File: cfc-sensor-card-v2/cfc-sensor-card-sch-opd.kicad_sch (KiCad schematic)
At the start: 69 parts, among them Q1 DMP2240UDM, Q2 DMN2050LQ-7, Q3 DMP3050LVT-7, Q4 DMPH2040UVTQ-7, Q5 DMN2050LQ-7, U1 MIC842LYC5, U2 MIC842LYC5, U3 MAX7310ATE+, U4 MAX4211FETE

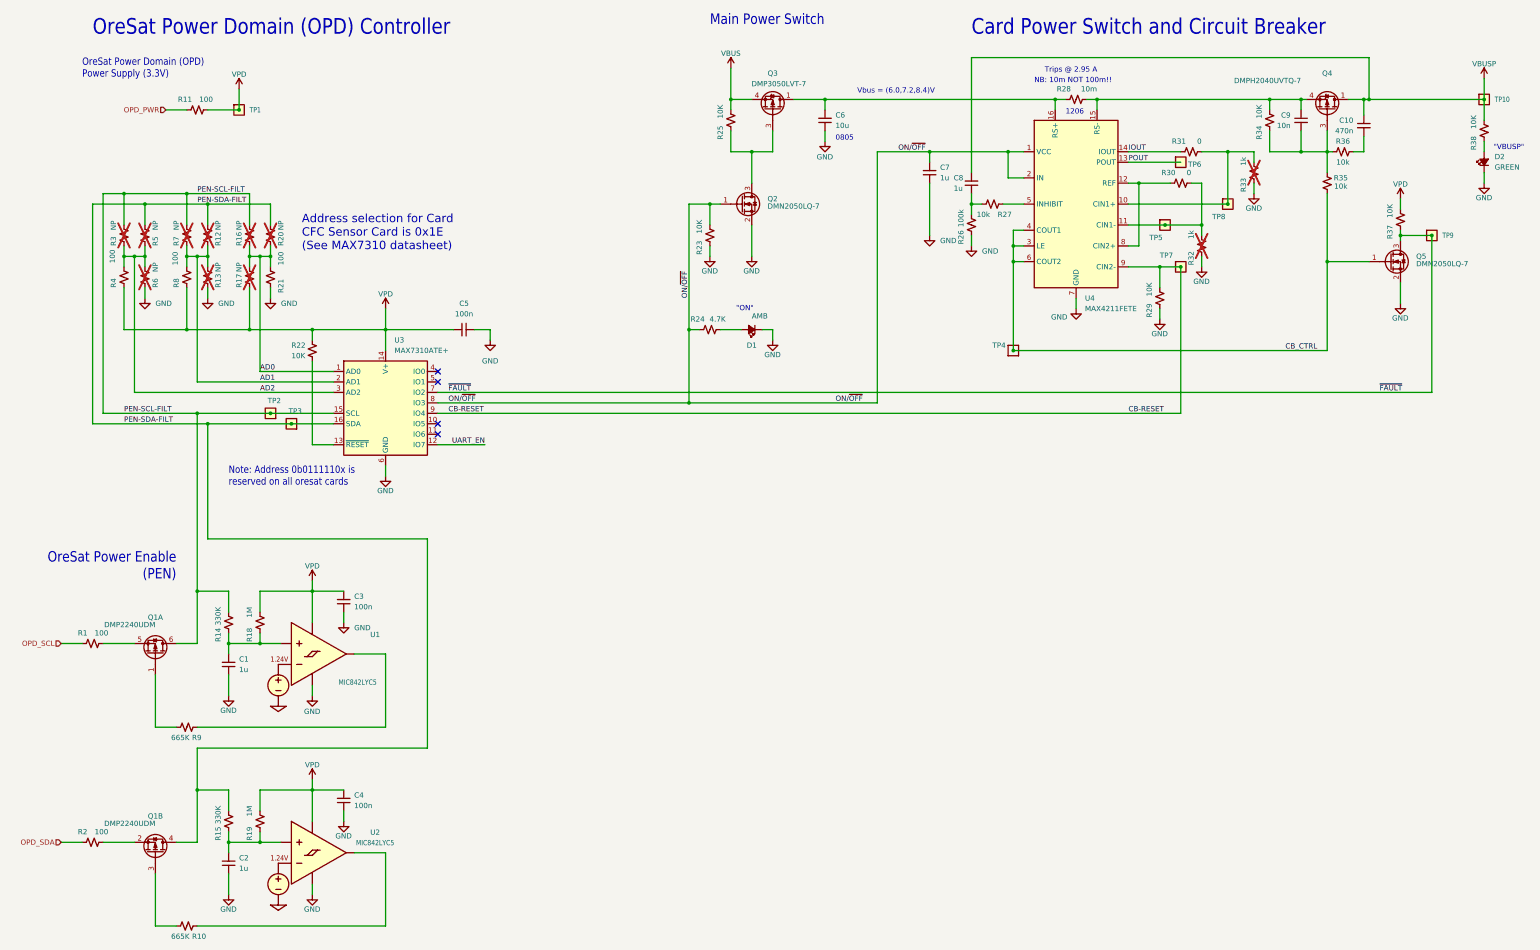
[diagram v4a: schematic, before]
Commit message: Update
Updated BOM, couple of fixes on OPD. Minor routing and layout changes. Removed logic gates from sensor card.
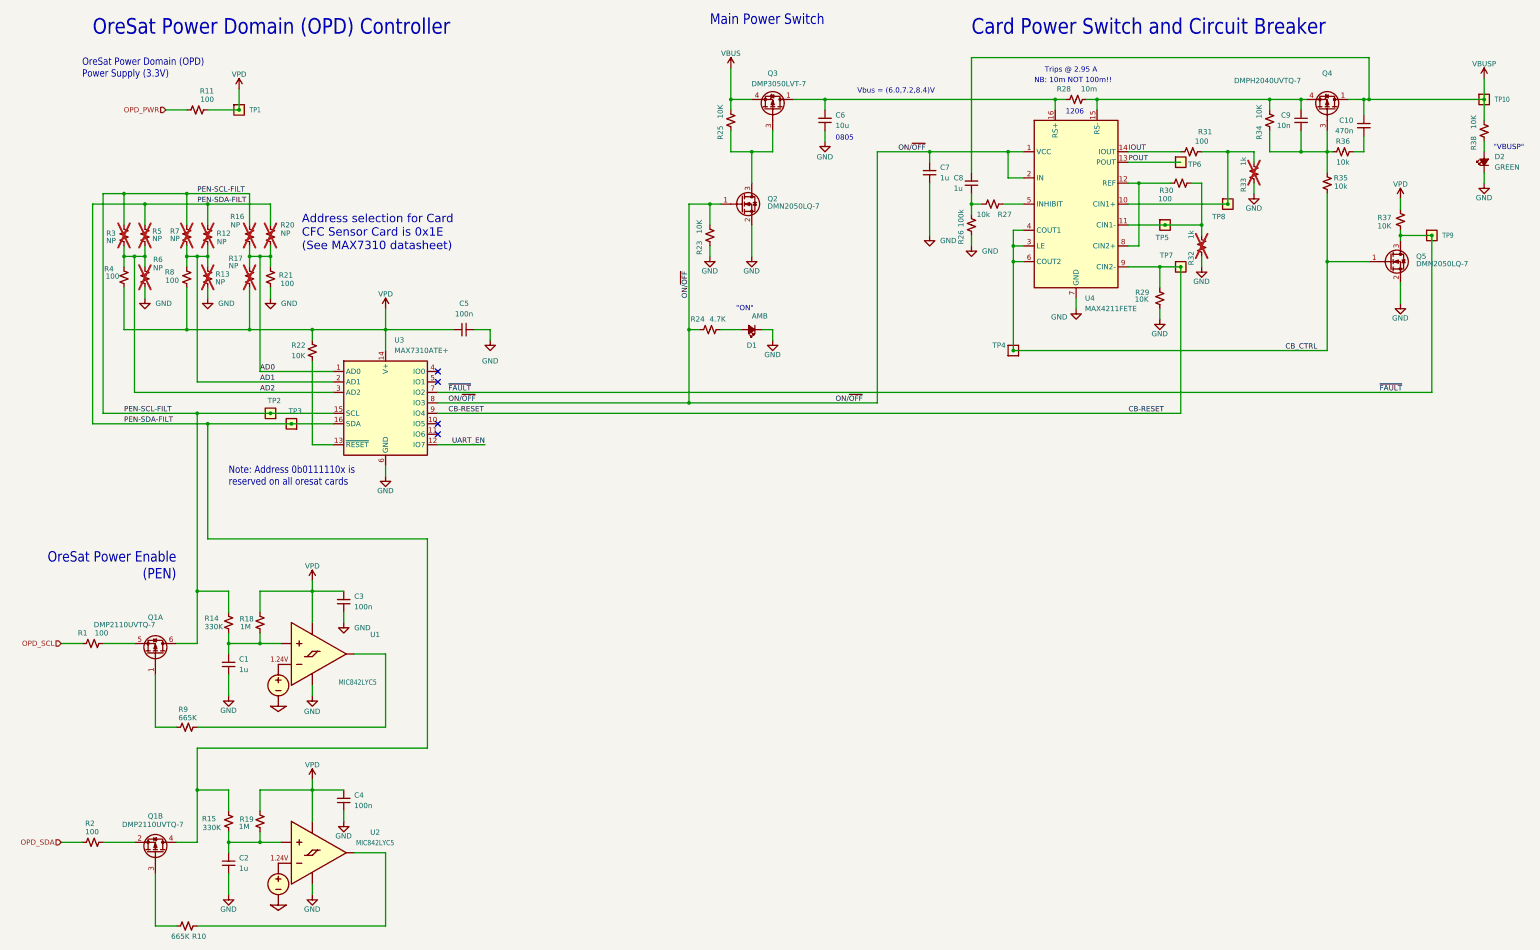
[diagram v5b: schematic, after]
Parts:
- Q1: value DMP2240UDM -> DMP2110UVTQ-7; DPN DMP2240UDMDICT-ND -> 31-DMP2110UVTQ-7CT-ND; MFR Diodes Inc -> Diodes Incorporated; MPN DMP2240UDM -> DMP2110UVTQ-7
- R12, R13, R16, R17, R20, R32, R33, R5, R6: footprint Resistor_SMD:R_0603_1608Metric_Pad0.98x0.95mm_HandSolder -> oresat-passives:0603-C-NOSILK
- R30, R31: value 0 -> 100; DPN RMCF0603ZT0R00CT-ND -> RMCF0603FT100RCT-ND; MPN RMCF0603ZT0R00 -> RMCF0603FT100R
